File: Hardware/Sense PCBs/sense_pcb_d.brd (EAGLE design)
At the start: 17.5 x 233 mm, 29 parts, among them J1 DF11-16DP-2DSA(01)

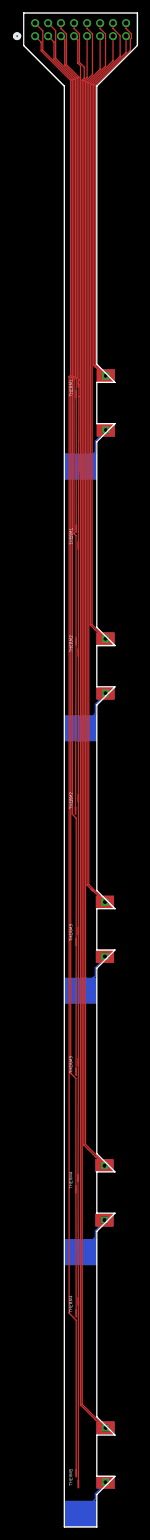
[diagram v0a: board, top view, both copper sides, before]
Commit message: fixed outline, updated gerbers
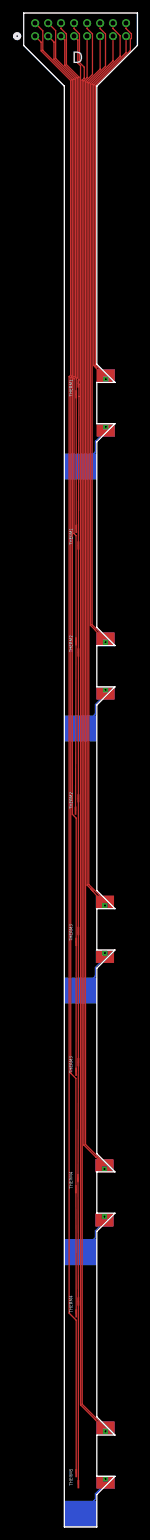
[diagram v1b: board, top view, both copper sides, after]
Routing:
- net N$9: track 273.4 -> 274.3 mm
- net N$7: track 193.1 -> 194.0 mm
- net N$1: track 113.1 -> 113.9 mm
- net N$3: track 434.8 -> 435.6 mm
- net N$5: track 7.20 -> 7.71 mm
- net N$4: track 6.46 -> 6.96 mm
- net N$2: track 6.44 -> 6.94 mm
- net N$6: track 6.80 -> 7.31 mm
- net N$8: track 7.01 -> 7.51 mm
- net N$10: track 353.1 -> 353.6 mm
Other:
- board text added: "D"
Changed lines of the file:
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@@
 <drawing>
 <settings>
-<setting alwaysvectorfont="no"/>
+<setting alwaysvectorfont="yes"/>
 <setting verticaltext="up"/>
 </settings>
@@
 <layer number="43" name="vRestrict" color="2" fill="10" visible="yes" active="yes"/>
 <layer number="44" name="Drills" color="7" fill="1" visible="no" active="yes"/>
-<layer number="45" name="Holes" color="7" fill="1" visible="no" active="yes"/>
+<layer number="45" name="Holes" color="7" fill="1" visible="yes" active="yes"/>
 <layer number="46" name="Milling" color="3" fill="1" visible="no" active="yes"/>
 <layer number="47" name="Measures" color="7" fill="1" visible="no" active="yes"/>
@@
 <text x="1.27" y="33.02" size="0.508" layer="21" font="vector" rot="R90">THERM4</text>
 <text x="1.27" y="6.35" size="0.508" layer="21" font="vector" rot="R90">THERM5</text>
+<text x="1.1938" y="225.298" size="1.778" layer="21">D</text>
 </plain>
 <attributes>
@@
 <wire x1="4.7836" y1="4.2756" x2="4.7836" y2="5.0896375" width="0.127" layer="16"/>
 <wire x1="4.7836" y1="5.0896375" x2="6.35" y2="6.6560375" width="0.127" layer="16"/>
-<wire x1="6.35" y1="6.6560375" x2="6.35" y2="6.89" width="0.127" layer="16"/>
+<wire x1="6.35" y1="6.6560375" x2="6.35" y2="7.398" width="0.127" layer="16"/>
+<wire x1="6.35" y1="6.89" x2="6.35" y2="6.89" width="0" layer="19" extent="1-16"/>
+<wire x1="6.35" y1="7.398" x2="6.35" y2="6.89" width="0" layer="19" extent="16-16"/>
 </signal>
 <signal name="N$4">
@@
 <wire x1="4.7836" y1="44.5436" x2="4.7836" y2="45.5896375" width="0.127" layer="16"/>
 <wire x1="4.7836" y1="45.5896375" x2="6.1722" y2="46.9782375" width="0.127" layer="16"/>
-<wire x1="6.1722" y1="46.9782375" x2="6.1722" y2="47.2506" width="0.127" layer="16"/>
+<wire x1="6.1722" y1="46.9782375" x2="6.1722" y2="47.7586" width="0.127" layer="16"/>
+<wire x1="6.1722" y1="47.2506" x2="6.1722" y2="47.2506" width="0" layer="19" extent="1-16"/>
+<wire x1="6.1722" y1="47.7586" x2="6.1722" y2="47.2506" width="0" layer="19" extent="16-16"/>
 </signal>
 <signal name="N$6">
@@
 <wire x1="4.7836" y1="84.7936" x2="4.7836" y2="86.0896375" width="0.127" layer="16"/>
 <wire x1="4.7836" y1="86.0896375" x2="6.2484" y2="87.5544375" width="0.127" layer="16"/>
-<wire x1="6.2484" y1="87.5544375" x2="6.2484" y2="87.8144" width="0.127" layer="16"/>
+<wire x1="6.2484" y1="87.5544375" x2="6.2484" y2="88.3224" width="0.127" layer="16"/>
+<wire x1="6.2484" y1="87.8144" x2="6.2484" y2="87.8144" width="0" layer="19" extent="1-16"/>
+<wire x1="6.2484" y1="88.3224" x2="6.2484" y2="87.8144" width="0" layer="19" extent="16-16"/>
 </signal>
 <signal name="N$8">
@@
 <wire x1="4.7836" y1="125.1436" x2="4.7836" y2="126.5896375" width="0.127" layer="16"/>
 <wire x1="4.7836" y1="126.5896375" x2="6.35" y2="128.1560375" width="0.127" layer="16"/>
-<wire x1="6.35" y1="128.1560375" x2="6.35" y2="128.3274" width="0.127" layer="16"/>
+<wire x1="6.35" y1="128.1560375" x2="6.35" y2="128.8354" width="0.127" layer="16"/>
+<wire x1="6.35" y1="128.3274" x2="6.35" y2="128.3274" width="0" layer="19" extent="1-16"/>
+<wire x1="6.35" y1="128.8354" x2="6.35" y2="128.3274" width="0" layer="19" extent="16-16"/>
 </signal>
 <signal name="THERM1">
 <contactref element="U$22" pad="P$1"/>
 <contactref element="U$23" pad="P$1"/>
-<contactref element="J1" pad="5"/>
 <contactref element="J1" pad="5"/>
 <wire x1="0.0635" y1="224.96503125" x2="1.9896" y2="223.03893125" width="0.127" layer="1"/>
@@
 <contactref element="U$24" pad="P$1"/>
 <contactref element="U$25" pad="P$1"/>
-<contactref element="J1" pad="4"/>
 <contactref element="J1" pad="4"/>
 <wire x1="-2.4892" y1="231.4448" x2="-1.3335" y2="230.2891" width="0.127" layer="1"/>
@@
 <contactref element="U$27" pad="P$1"/>
 <contactref element="J1" pad="3"/>
-<contactref element="J1" pad="3"/>
 <wire x1="-2.4892" y1="229.4382" x2="-1.5875" y2="228.5365" width="0.127" layer="1"/>
 <wire x1="-1.5875" y1="228.5365" x2="-1.5875" y2="225.89760625" width="0.127" layer="1"/>
@@
 <contactref element="U$28" pad="P$1"/>
 <contactref element="U$29" pad="P$1"/>
-<contactref element="J1" pad="2"/>
 <contactref element="J1" pad="2"/>
 <wire x1="-4.4958" y1="231.4448" x2="-3.3147" y2="230.2637" width="0.127" layer="1"/>
@@
 <signal name="THERM5">
 <contactref element="U$30" pad="P$1"/>
-<contactref element="J1" pad="1"/>
 <contactref element="J1" pad="1"/>
 <wire x1="-3.5687" y1="227.16038125" x2="0.9736" y2="222.61808125" width="0.127" layer="1"/>
@@
 <wire x1="3.06513125" y1="224.6589875" x2="3.06513125" y2="222.99486875" width="0.127" layer="1"/>
 <wire x1="3.06513125" y1="222.99486875" x2="2.7516" y2="222.6813375" width="0.127" layer="1"/>
-<wire x1="6.35" y1="15.2939625" x2="6.35" y2="15.24" width="0.127" layer="1"/>
+<wire x1="6.35" y1="15.2939625" x2="6.35" y2="14.732" width="0.127" layer="1"/>
 <wire x1="2.7516" y1="222.6813375" x2="2.7516" y2="18.8923625" width="0.127" layer="1"/>
 <wire x1="2.7516" y1="18.8923625" x2="6.35" y2="15.2939625" width="0.127" layer="1"/>
-<wire x1="4.774975" y1="16.509775" x2="6.35" y2="15.24" width="0.127" layer="1"/>
+<wire x1="4.774975" y1="16.509775" x2="6.35" y2="14.732" width="0.127" layer="1"/>
+<wire x1="6.35" y1="15.24" x2="6.35" y2="15.24" width="0" layer="19" extent="1-16"/>
+<wire x1="6.35" y1="14.732" x2="6.35" y2="15.24" width="0" layer="19" extent="16-16"/>
 </signal>
 <signal name="N$5">
@@
 <wire x1="4.7836" y1="165.4436" x2="4.7836" y2="167.0896375" width="0.127" layer="16"/>
 <wire x1="4.7836" y1="167.0896375" x2="6.3754" y2="168.6814375" width="0.127" layer="16"/>
-<wire x1="6.3754" y1="168.6814375" x2="6.3754" y2="168.815" width="0.127" layer="16"/>
+<wire x1="6.3754" y1="168.6814375" x2="6.3754" y2="169.323" width="0.127" layer="16"/>
+<wire x1="6.3754" y1="168.815" x2="6.3754" y2="168.815" width="0" layer="19" extent="1-16"/>
+<wire x1="6.3754" y1="169.323" x2="6.3754" y2="168.815" width="0" layer="19" extent="16-16"/>
 </signal>
 <signal name="N$1">
@@
 <wire x1="10.16" y1="227.2160375" x2="4.7836" y2="221.8396375" width="0.127" layer="1"/>
 <wire x1="4.7836" y1="178.8603625" x2="6.3754" y2="177.2685625" width="0.127" layer="1"/>
-<wire x1="6.3754" y1="177.2685625" x2="6.3754" y2="177.165" width="0.127" layer="1"/>
+<wire x1="6.3754" y1="177.2685625" x2="6.3754" y2="176.657" width="0.127" layer="1"/>
 <wire x1="10.16" y1="228.9311625" x2="10.16" y2="227.2160375" width="0.127" layer="1"/>
 <wire x1="4.5296" y1="221.94485" x2="4.5296" y2="178.75515" width="0.127" layer="1"/>
@@
 <wire x1="9.4996" y1="229.4382" x2="9.4996" y2="226.91485" width="0.127" layer="1"/>
 <wire x1="9.4996" y1="226.91485" x2="4.5296" y2="221.94485" width="0.127" layer="1"/>
-<wire x1="4.647375" y1="178.637375" x2="6.3754" y2="177.165" width="0.127" layer="1"/>
+<wire x1="4.647375" y1="178.637375" x2="6.3754" y2="176.657" width="0.127" layer="1"/>
+<wire x1="6.3754" y1="177.165" x2="6.3754" y2="177.165" width="0" layer="19" extent="1-16"/>
+<wire x1="6.3754" y1="176.657" x2="6.3754" y2="177.165" width="0" layer="19" extent="16-16"/>
 </signal>
 <signal name="N$7">
@@
 <wire x1="8.58776875" y1="229.51086875" x2="8.58776875" y2="226.36223125" width="0.127" layer="1"/>
 <wire x1="8.58776875" y1="226.36223125" x2="4.2756" y2="222.0500625" width="0.127" layer="1"/>
-<wire x1="6.35" y1="136.7939625" x2="6.35" y2="136.6774" width="0.127" layer="1"/>
+<wire x1="6.35" y1="136.7939625" x2="6.35" y2="136.1694" width="0.127" layer="1"/>
 <wire x1="4.2756" y1="222.0500625" x2="4.2756" y2="138.8683625" width="0.127" layer="1"/>
 <wire x1="4.2756" y1="138.8683625" x2="6.35" y2="136.7939625" width="0.127" layer="1"/>
-<wire x1="4.666575" y1="138.118175" x2="6.35" y2="136.6774" width="0.127" layer="1"/>
+<wire x1="4.666575" y1="138.118175" x2="6.35" y2="136.1694" width="0.127" layer="1"/>
+<wire x1="6.35" y1="136.6774" x2="6.35" y2="136.6774" width="0" layer="19" extent="1-16"/>
+<wire x1="6.35" y1="136.1694" x2="6.35" y2="136.6774" width="0" layer="19" extent="16-16"/>
 </signal>
 <signal name="N$9">
@@
 <wire x1="5.5118" y1="230.6056375" x2="6.3373" y2="229.7801375" width="0.127" layer="1"/>
 <wire x1="6.3373" y1="229.7801375" x2="6.3373" y2="224.8301875" width="0.127" layer="1"/>
-<wire x1="6.2484" y1="96.3955625" x2="6.2484" y2="96.1644" width="0.127" layer="1"/>
+<wire x1="6.2484" y1="96.3955625" x2="6.2484" y2="95.6564" width="0.127" layer="1"/>
 <wire x1="3.7676" y1="222.2604875" x2="3.7676" y2="98.8763625" width="0.127" layer="1"/>
 <wire x1="3.7676" y1="98.8763625" x2="6.2484" y2="96.3955625" width="0.127" layer="1"/>
 <wire x1="6.3373" y1="224.8301875" x2="3.7676" y2="222.2604875" width="0.127" layer="1"/>
-<wire x1="4.152375" y1="98.132375" x2="6.2484" y2="96.1644" width="0.127" layer="1"/>
+<wire x1="4.152375" y1="98.132375" x2="6.2484" y2="95.6564" width="0.127" layer="1"/>
+<wire x1="6.2484" y1="96.1644" x2="6.2484" y2="96.1644" width="0" layer="19" extent="1-16"/>
+<wire x1="6.2484" y1="95.6564" x2="6.2484" y2="96.1644" width="0" layer="19" extent="16-16"/>
 </signal>
 <signal name="N$10">
@@
 <wire x1="4.3307" y1="223.5420125" x2="3.2596" y2="222.4709125" width="0.127" layer="1"/>
 <wire x1="6.1722" y1="55.9717625" x2="6.1722" y2="55.88" width="0.127" layer="1"/>
-<wire x1="6.1722" y1="55.88" x2="6.1722" y2="55.6006" width="0.127" layer="1"/>
+<wire x1="6.1722" y1="55.88" x2="6.1722" y2="55.0926" width="0.127" layer="1"/>
 <wire x1="3.2596" y1="58.8843625" x2="6.1722" y2="55.9717625" width="0.127" layer="1"/>
 <wire x1="3.2596" y1="222.4709125" x2="3.2596" y2="58.8843625" width="0.127" layer="1"/>
 <wire x1="4.857375" y1="56.927375" x2="6.1722" y2="55.88" width="0.127" layer="1"/>
+<wire x1="6.1722" y1="55.6006" x2="6.1722" y2="55.6006" width="0" layer="19" extent="1-16"/>
+<wire x1="6.1722" y1="55.0926" x2="6.1722" y2="55.6006" width="0" layer="19" extent="16-16"/>
 </signal>
 </signals>
